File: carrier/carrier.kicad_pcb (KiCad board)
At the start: 4 copper layers, 9.2 x 7.4 mm, 2 parts, among them J1 DF40GB-30DP-0.4V(51), U1 TC58NVG1S3HBAI6

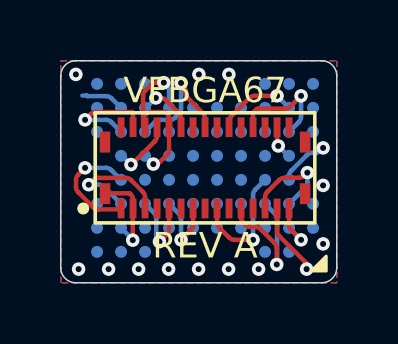
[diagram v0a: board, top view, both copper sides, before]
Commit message: Route base for the 4.0mm mezzanine and the SMT DIP48 field
Copper follow-up to f02e7d7, which changed only symbols, schematics and
footprints. Both boards now carry the new parts.

carrier: J1 swapped to DF40TC-30DP-0.4V(51). All 30 signal pads landed on
their exact previous coordinates, so nothing was re-routed; the four G1-G4
retention-tab pads are gone. 0 DRC violations, 0 unconnected. Panel
regenerated.

base: J1 swapped to DF40TC(4.0)-30DS-0.4V(51), same story. J2 swapped to
the surface-mount socket-strip field; its 48 pads keep their Y coordinates
and stagger +-1.65 mm about the unchanged row centrelines.

The interesting part is what SMD pads cost. They live on F.Cu only, and
this board's copper arrived at the old through-hole pads from all four
layers -- F.Cu on 4 pins, B.Cu on 7, In1 on 6, In2 on 3. Rather than
re-plan the whole board, route_base.py now gives every used J2 pad a
0.15 mm F.Cu stub back to its row centreline and a 0.45/0.20 via there.
The via sits exactly where the through-hole pad centre used to be, which
is the coordinate every existing route and the planner already target. 19
pads, and connectivity came back without moving a single destination.
The 1.4 mm gap between the staggered pad columns takes that via with
0.475 mm of copper clearance against a 0.1 mm rule.

Also in route_base.py: VCC now falls back from J2.37 to J2.12, and pin 10
routes before pin 6 so pin 6 can be offered pin 10's via.

The four passives moved 0.5 mm left with their track endpoints. They were
placed against a through-hole field whose copper started 1.8 mm further
right; the SMT pads brought J2's copper out to x=113.88 and the 0603
courtyards overlapped it. Copper clearance was still legal at 0.168 mm --
this was a courtyard fix, not an electrical one.

base is 0 DRC violations, 6 unconnected, both understood and documented
in HANDOFF:
  - J1.6 (VCC) is walled in on B.Cu by IO5's and IO7's hand routes, which
    pass 0.4 mm away -- exactly the via limit -- leaving i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
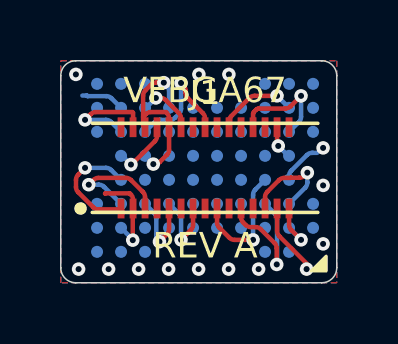
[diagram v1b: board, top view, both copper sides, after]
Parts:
- J1: value DF40GB-30DP-0.4V(51) -> DF40TC-30DP-0.4V(51); footprint Connector_Hirose_DF40:HIROSE_DF40GB-30DP-0.4V_51_ -> Connector_Hirose_DF40:HIROSE_DF40TC-30DP-0.4V_51_
